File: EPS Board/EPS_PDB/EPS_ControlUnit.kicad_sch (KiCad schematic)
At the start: 41 parts, among them Q1 PMOS, Q2 NMOS, SW1 SW_SPDT, U2 MCP2551-I-P, U3 MCP2551-I-P, U4 STM32L476VET6, U5 TPS3824-33QDBVRQ1, Y1 32MHz

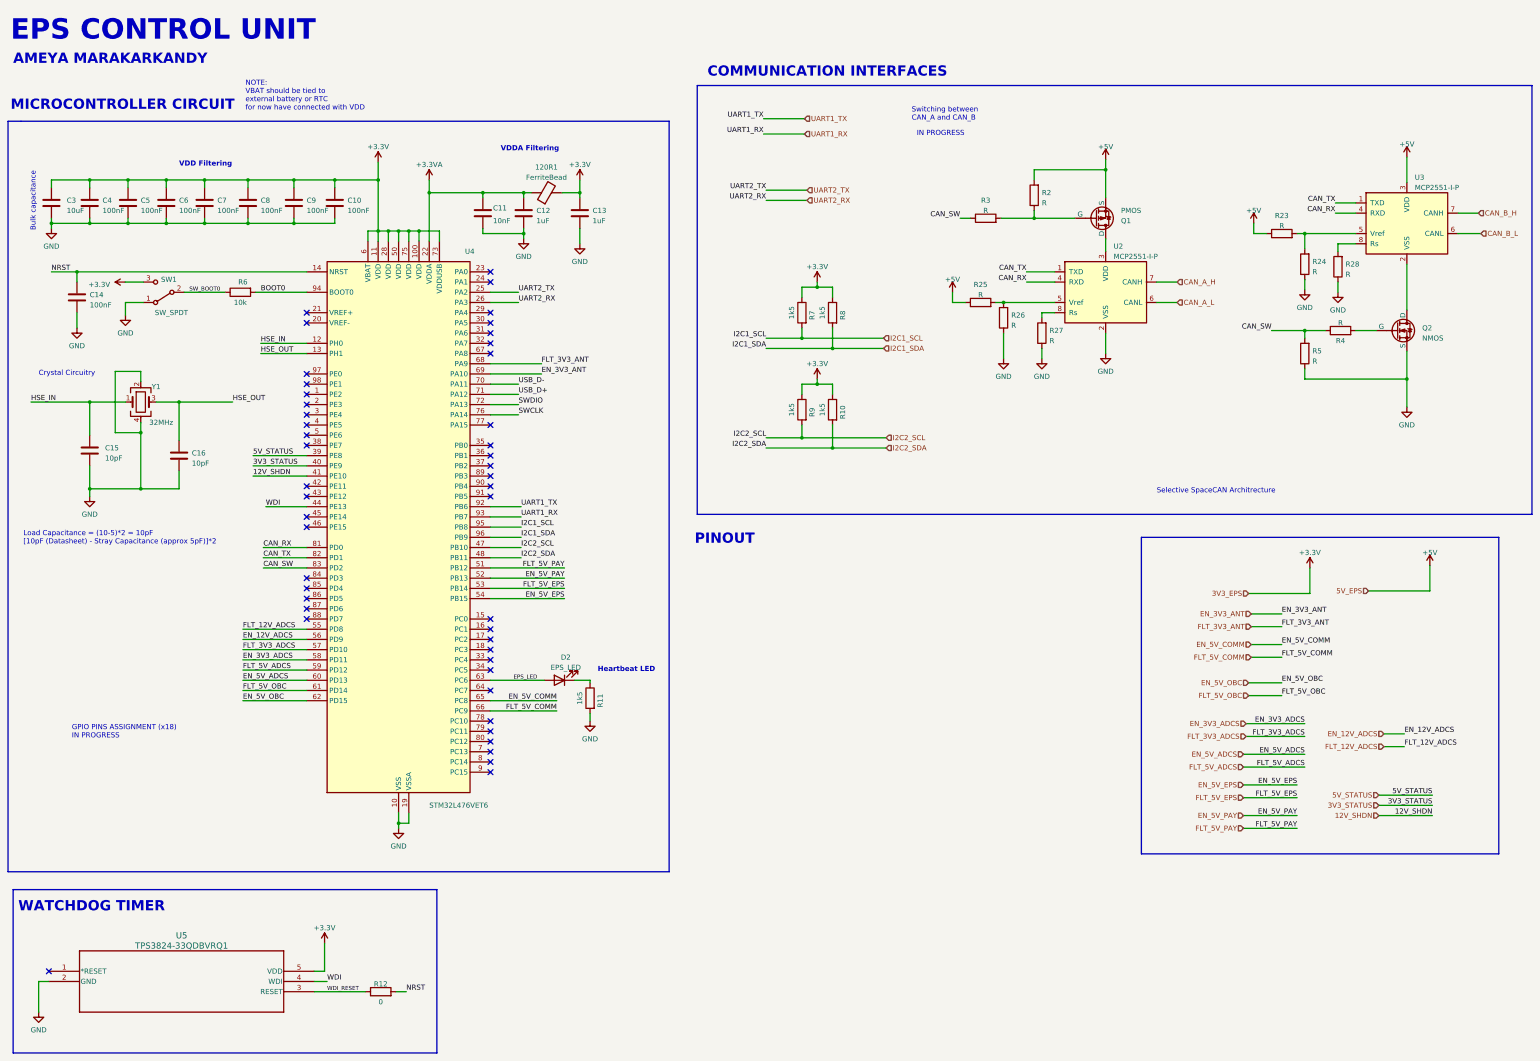
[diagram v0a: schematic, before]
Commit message: Changed CAN Transceiver IC
Chose an ic which can operate at 5V Vcc and 3.3V logic
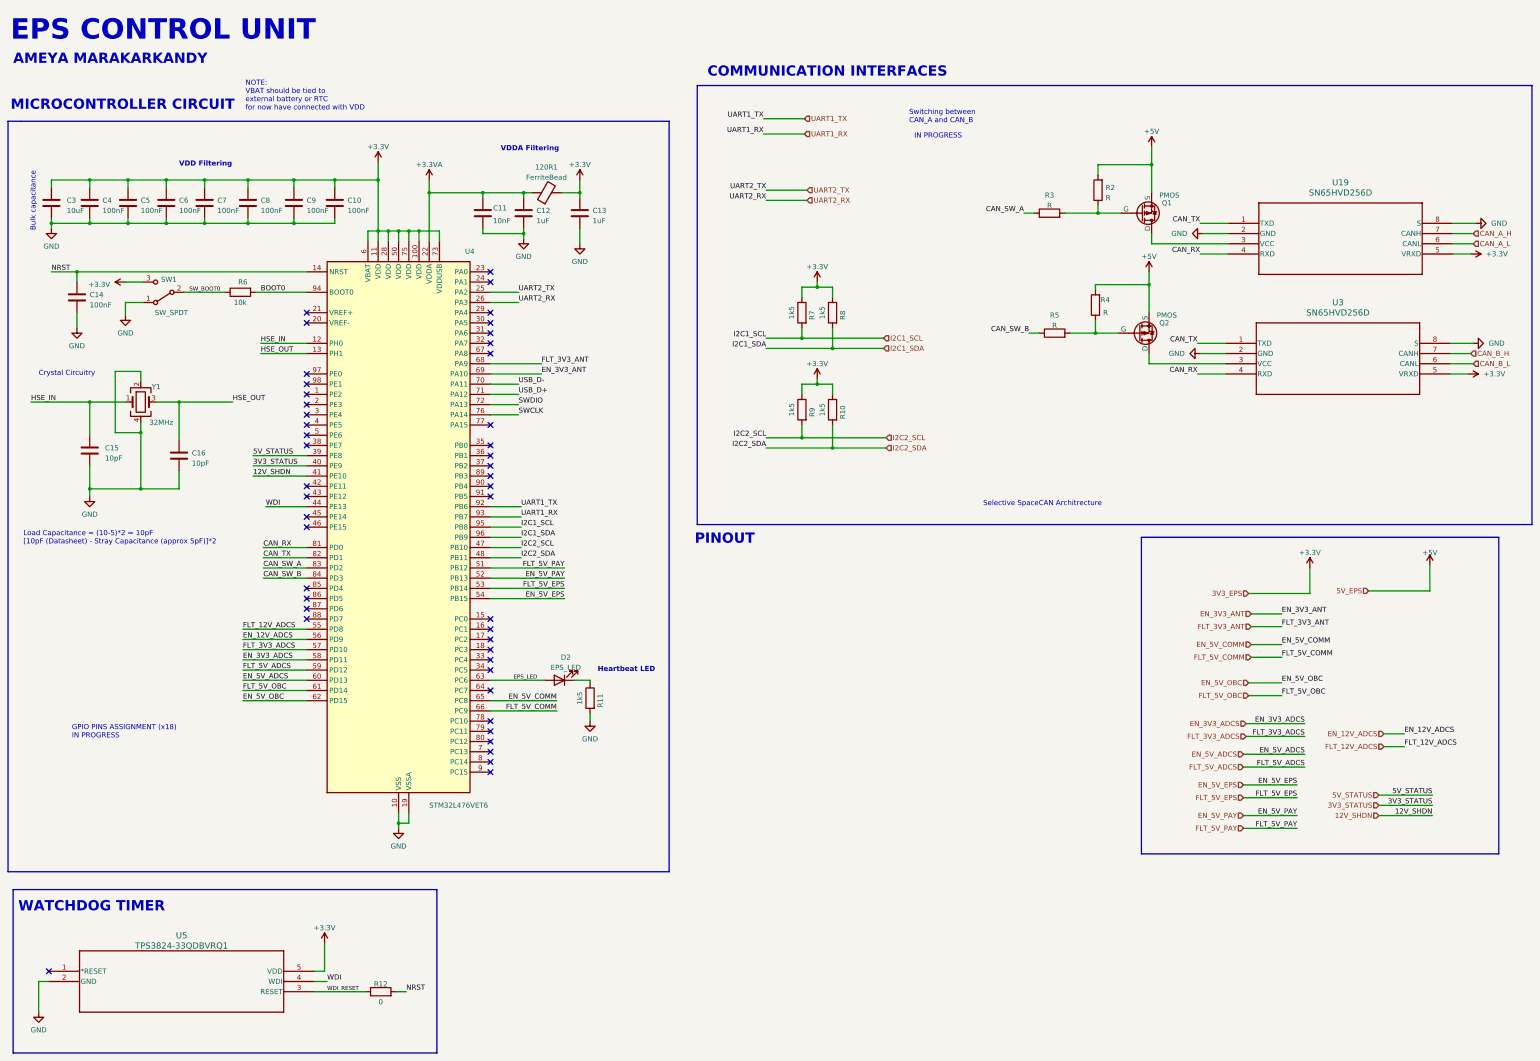
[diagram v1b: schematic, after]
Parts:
- removed Q2: NMOS, symbol Simulation_SPICE:NMOS
- removed R23, R24, R25, R26, R27, R28: R, symbol Device:R
- removed U2, U3: MCP2551-I-P, Package_SO:SOIC-8_3.9x4.9mm_P1.27mm, symbol Interface_CAN_LIN:MCP2551-I-SN
- added Q2: PMOS, symbol Simulation_SPICE:PMOS
- added U19, U3: SN65HVD256D, D8, symbol SN65HVD256D:SN65HVD256D
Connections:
- net +3.3V: now also U19.5 (VRXD), U3.5 (VRXD)
- net +5V: now also R4.2, Q2.3 (S)
- net CAN_A_H: now also U19.7 (CANH)
- net CAN_A_L: now also U19.6 (CANL)
- net CAN_B_H: now also U3.7 (CANH)
- net CAN_B_L: now also U3.6 (CANL)
- net CAN_RX: now also U19.4 (RXD), U3.4 (RXD)
- net CAN_TX: now also U19.1 (TXD), U3.1 (TXD)
- net GND: now also U19.2 (GND), U19.8 (S), U3.2 (GND), U3.8 (S); no longer R5.1
- net at Q1.1 (D): now also U19.3 (VCC)
- net CAN_SW_B: now reaches U4.84 (PD3)
- net CAN_SW_B: now also R5.1
- net CAN_SW: no longer names the net of R4.1, R5.2
- net CAN_SW: now also Q2.2 (G); no longer R3.1, U4.83 (PD2)
- new net: Q2.1 (D), U3.3 (VCC)
- new net CAN_SW_A: R3.1, U4.83 (PD2)
- no-connect marks 47 -> 46
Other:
- moved on the sheet: Q1, R2, R3

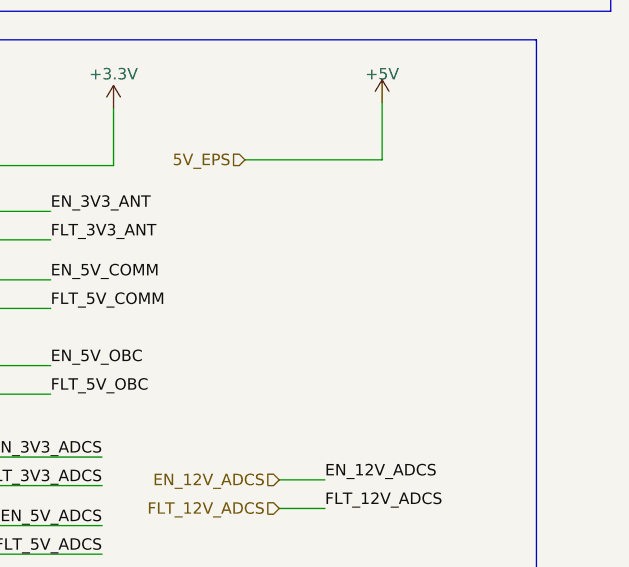
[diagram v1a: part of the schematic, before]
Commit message: Pin definitions of regulaton unit added to root and final changes commments added
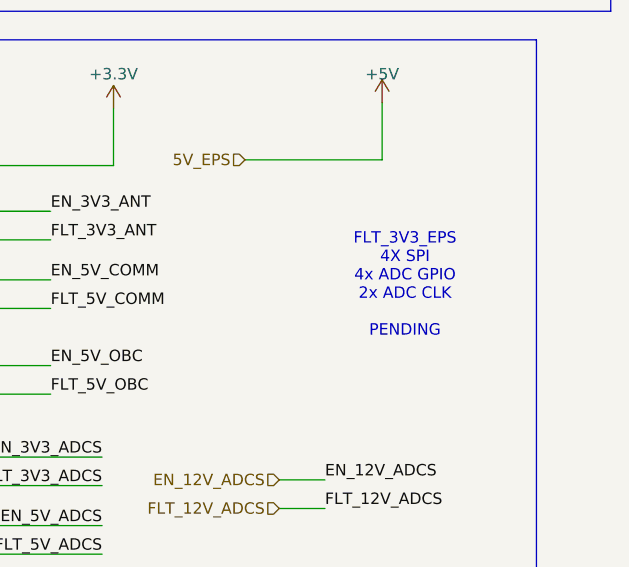
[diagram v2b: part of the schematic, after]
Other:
- note added: "FLT_3V3_EPS 4X SPI 4x ADC GPIO 2x ADC CLK PENDING"
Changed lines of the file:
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@@
+		)
+	)
+	(text "FLT_3V3_EPS\n4X SPI\n4x ADC GPIO\n2x ADC CLK\n\nPENDING"
+		(exclude_from_sim no)
+		(at 377.19 176.53 0)
+		(effects
+			(font
+				(size 1.27 1.27)
+			)
 		)
 	)

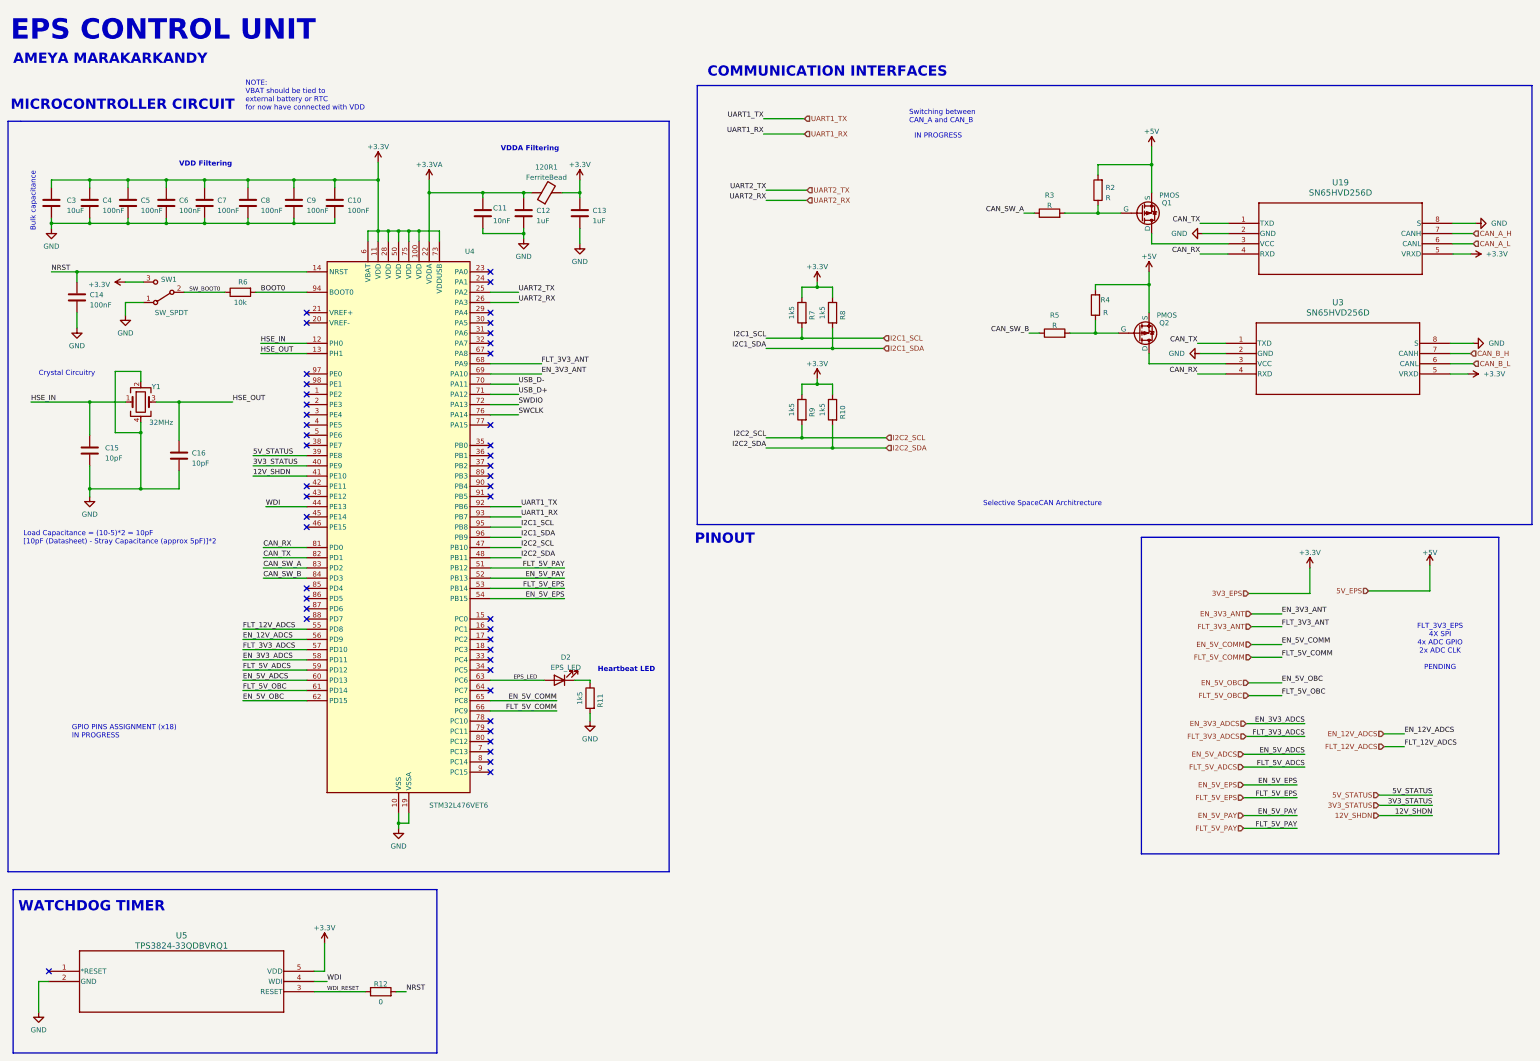
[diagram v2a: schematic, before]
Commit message: Interfaced Control and PD&R unit
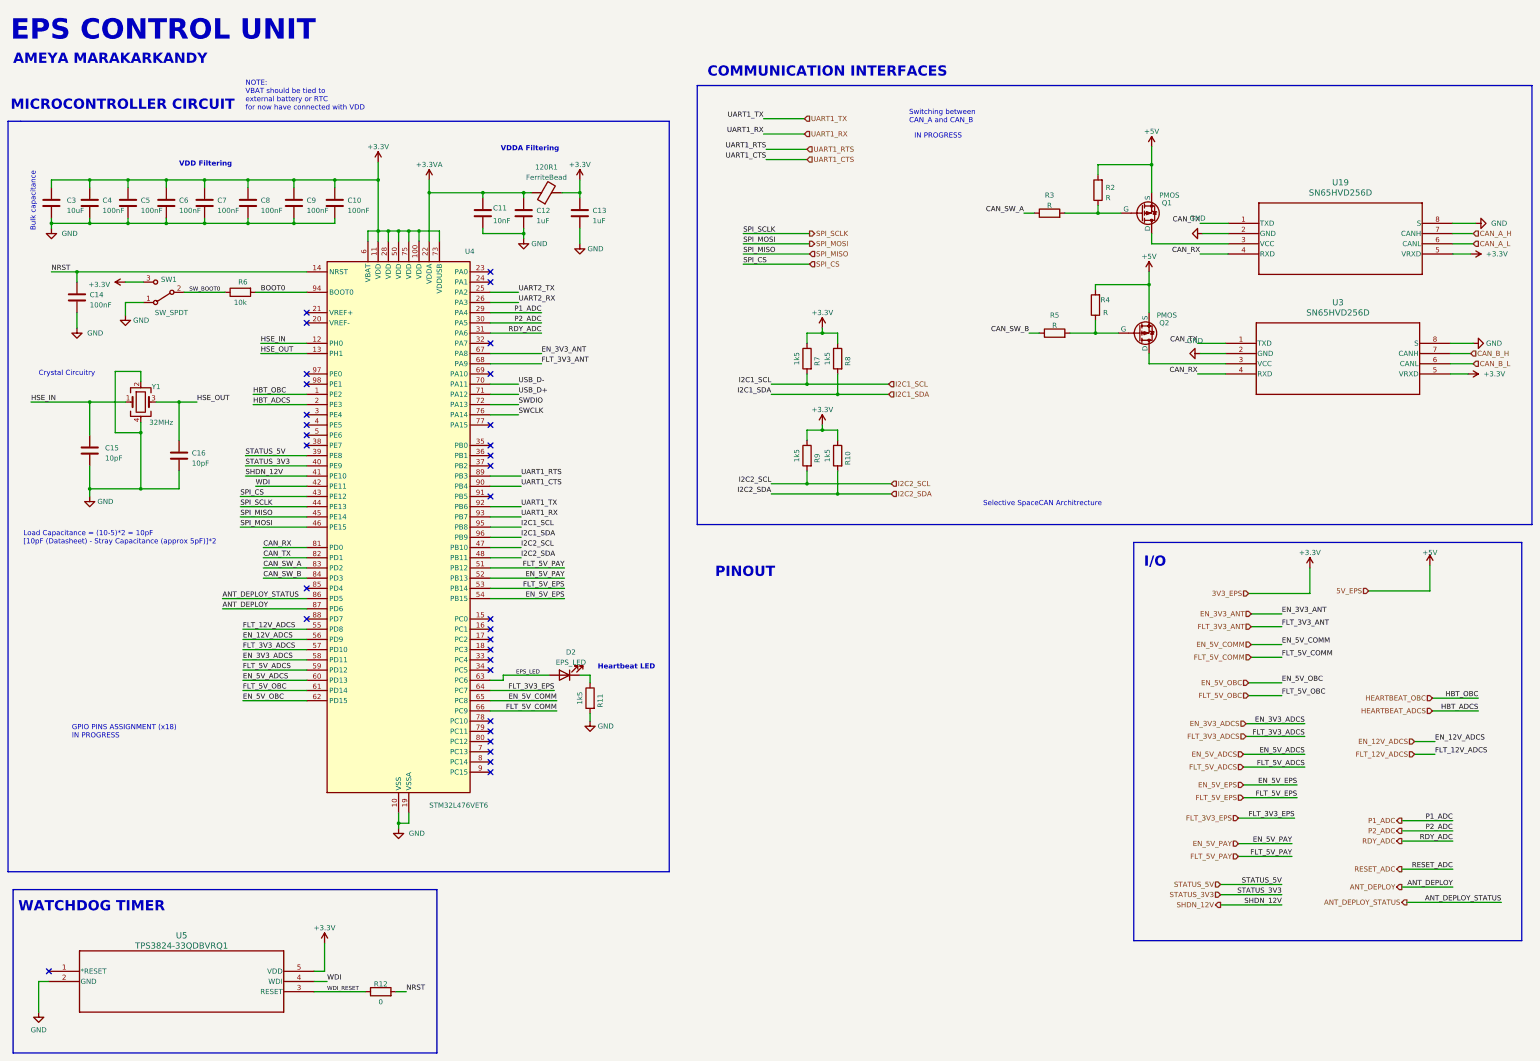
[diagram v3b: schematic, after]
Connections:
- net EN_3V3_ANT: now also U4.67 (PA8); no longer U4.69 (PA10)
- net WDI: now also U4.42 (PE11); no longer U4.44 (PE13)
- net HEARTBEAT_OBC: now reaches U4.1 (PE2)
- net HEARTBEAT_ADCS: now reaches U4.2 (PE3)
- net P1_ADC: now reaches U4.29 (PA4)
- net P2_ADC: now reaches U4.30 (PA5)
- net RDY_ADC: now reaches U4.31 (PA6)
- net SPI_CS: now reaches U4.43 (PE12)
- net SPI_MISO: now reaches U4.45 (PE14)
- net SPI_MOSI: now reaches U4.46 (PE15)
- net FLT_3V3_EPS: now reaches U4.64 (PC7)
- net ANT_DEPLOY_STATUS: now reaches U4.86 (PD5)
- net ANT_DEPLOY: now reaches U4.87 (PD6)
- net UART1_RTS: now reaches U4.89 (PB3)
- net UART1_CTS: now reaches U4.90 (PB4)
- net 12V_SHDN renamed SHDN_12V
- net 3V3_STATUS renamed STATUS_3V3
- net 5V_STATUS renamed STATUS_5V
- new net SPI_SCLK: U4.44 (PE13)
- no-connect marks 46 -> 32
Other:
- note added: "I/O"
- note removed: "FLT_3V3_EPS 4X SPI 4x ADC GPIO 2x ADC CLK PENDING"
- moved on the sheet: D2, R10, R7, R8, R9
